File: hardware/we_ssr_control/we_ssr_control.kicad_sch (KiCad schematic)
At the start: 6 parts

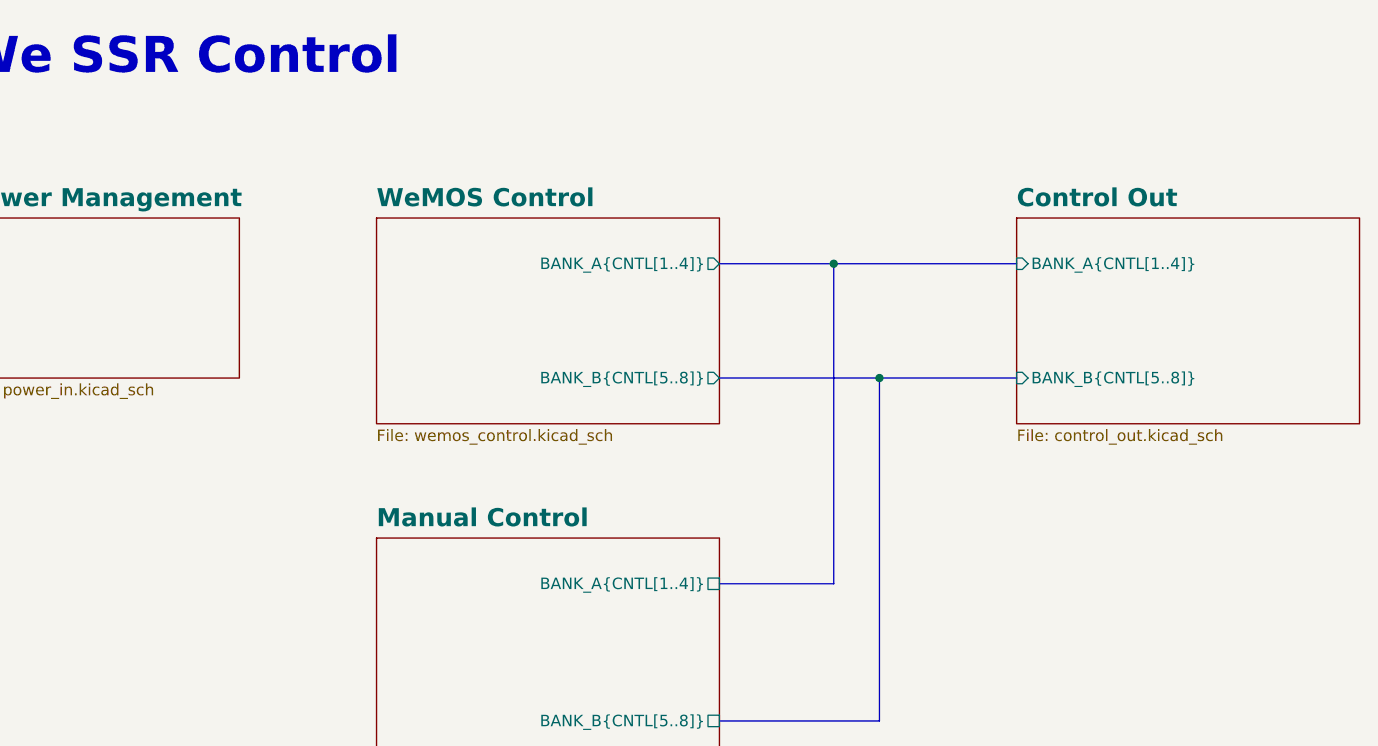
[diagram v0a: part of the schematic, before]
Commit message: Power supply changes plus misc.
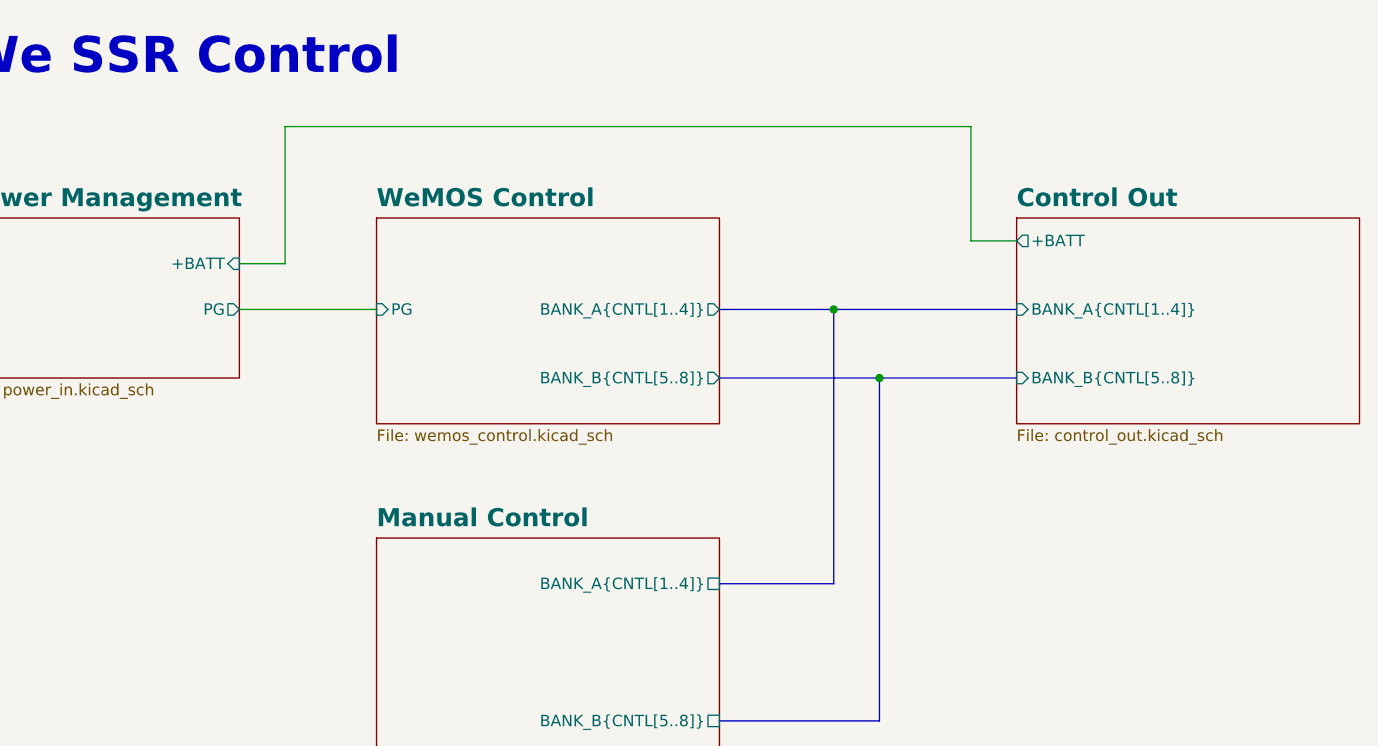
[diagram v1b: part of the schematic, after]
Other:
- sheet Control Out ports: added +BATT; removed none
- sheet Power Management ports: added +BATT, PG; removed none
- sheet WeMOS Control ports: added PG; removed none

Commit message: Pre KiCad 7.0.0 WIP
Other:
- sheet Control Out ports: added BANK_A{OUT[1..4]}, BANK_B{OUT[5..8]}; removed BANK_A{CNTL[1..4]}, BANK_B{CNTL[5..8]}
- sheet Manual Control ports: added BANK_A{OUT[1..4]}, BANK_B{OUT[5..8]}; removed BANK_A{CNTL[1..4]}, BANK_B{CNTL[5..8]}
- sheet WeMOS Control ports: added BANK_A{OUT[1..4]}, BANK_B{OUT[5..8]}; removed BANK_A{CNTL[1..4]}, BANK_B{CNTL[5..8]}
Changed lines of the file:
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@@
   (junction (at 27.94 152.4) (diameter 0) (color 0 0 0 0)
   )
-  (junction (at 111.76 45.72) (diameter 0) (color 0 0 0 0)
-  )
-  (junction (at 116.84 53.34) (diameter 0) (color 0 0 0 0)
+  (junction (at 111.76 45.72) (diameter 0) (color 255 255 0 1)
+  )
+  (junction (at 116.84 53.34) (diameter 0) (color 255 255 0 1)
   )
   (junction (at 27.94 157.48) (diameter 0) (color 0 0 0 0)
@@
   )
   (bus (pts (xy 99.06 45.72) (xy 111.76 45.72))
-    (stroke (width 0) (type default) (color 0 0 0 0))
+    (stroke (width 0) (type default) (color 255 255 0 1))
   )
   (wire (pts (xy 127 38.1) (xy 127 25.4))
@@
   )
   (bus (pts (xy 111.76 45.72) (xy 132.08 45.72))
-    (stroke (width 0) (type default) (color 0 0 0 0))
+    (stroke (width 0) (type default) (color 255 255 0 1))
   )
   (polyline (pts (xy 40.64 172.72) (xy 40.64 195.58))
@@
   )
   (bus (pts (xy 99.06 53.34) (xy 116.84 53.34))
-    (stroke (width 0) (type default) (color 0 0 0 0))
+    (stroke (width 0) (type default) (color 255 255 0 1))
   )
   (polyline (pts (xy 63.5 129.54) (xy 63.5 200.66))
@@
   )
   (bus (pts (xy 99.06 76.2) (xy 111.76 76.2))
-    (stroke (width 0) (type default) (color 0 0 0 0))
+    (stroke (width 0) (type default) (color 255 255 0 1))
   )
   (bus (pts (xy 116.84 91.44) (xy 116.84 53.34))
-    (stroke (width 0) (type default) (color 0 0 0 0))
+    (stroke (width 0) (type default) (color 255 255 0 1))
   )
   (polyline (pts (xy 63.5 200.66) (xy 15.24 200.66))
@@
   )
   (bus (pts (xy 116.84 53.34) (xy 132.08 53.34))
-    (stroke (width 0) (type default) (color 0 0 0 0))
+    (stroke (width 0) (type default) (color 255 255 0 1))
   )
   (polyline (pts (xy 45.72 137.16) (xy 45.72 167.64))
@@
   )
   (bus (pts (xy 99.06 91.44) (xy 116.84 91.44))
-    (stroke (width 0) (type default) (color 0 0 0 0))
+    (stroke (width 0) (type default) (color 255 255 0 1))
   )
   (bus (pts (xy 111.76 76.2) (xy 111.76 45.72))
-    (stroke (width 0) (type default) (color 0 0 0 0))
+    (stroke (width 0) (type default) (color 255 255 0 1))
   )
   (wire (pts (xy 27.94 147.32) (xy 27.94 152.4))
@@
       (effects (font (size 1.27 1.27)) (justify left top))
     )
-    (pin "BANK_B{CNTL[5..8]}" input (at 132.08 53.34 180)
-      (effects (font (size 1.27 1.27)) (justify left))
-    )
-    (pin "BANK_A{CNTL[1..4]}" input (at 132.08 45.72 180)
+    (pin "BANK_B{OUT[5..8]}" input (at 132.08 53.34 180)
+      (effects (font (size 1.27 1.27)) (justify left))
+    )
+    (pin "BANK_A{OUT[1..4]}" input (at 132.08 45.72 180)
       (effects (font (size 1.27 1.27)) (justify left))
     )
@@
       (effects (font (size 1.27 1.27)) (justify left top))
     )
-    (pin "BANK_A{CNTL[1..4]}" passive (at 99.06 76.2 0)
-      (effects (font (size 1.27 1.27)) (justify right))
-    )
-    (pin "BANK_B{CNTL[5..8]}" passive (at 99.06 91.44 0)
+    (pin "BANK_A{OUT[1..4]}" passive (at 99.06 76.2 0)
+      (effects (font (size 1.27 1.27)) (justify right))
+    )
+    (pin "BANK_B{OUT[5..8]}" passive (at 99.06 91.44 0)
       (effects (font (size 1.27 1.27)) (justify right))
     )
@@
       (effects (font (size 1.27 1.27)) (justify left top))
     )
-    (pin "BANK_A{CNTL[1..4]}" output (at 99.06 45.72 0)
-      (effects (font (size 1.27 1.27)) (justify right))
-    )
-    (pin "BANK_B{CNTL[5..8]}" output (at 99.06 53.34 0)
+    (pin "BANK_A{OUT[1..4]}" output (at 99.06 45.72 0)
+      (effects (font (size 1.27 1.27)) (justify right))
+    )
+    (pin "BANK_B{OUT[5..8]}" output (at 99.06 53.34 0)
       (effects (font (size 1.27 1.27)) (justify right))
     )
@@
     )
     (path "/a6fe8e39-c8fe-4793-ba2c-9e580a74c2e6/3fb71cbf-cff9-4475-be5c-cf772014cc05"
-      (reference "QD1") (unit 1) (value "2N7002K") (footprint "Package_TO_SOT_SMD:SOT-23-3")
+      (reference "QD1") (unit 1) (value "2N7002K") (footprint "dragon_mobile:2V7002KT1G")
     )
     (path "/a6fe8e39-c8fe-4793-ba2c-9e580a74c2e6/c9bf8404-861c-4866-b68d-e32ad5305808"
-      (reference "QD2") (unit 1) (value "2N7002K") (footprint "Package_TO_SOT_SMD:SOT-23-3")
+      (reference "QD2") (unit 1) (value "2N7002K") (footprint "dragon_mobile:2V7002KT1G")
     )
     (path "/a6fe8e39-c8fe-4793-ba2c-9e580a74c2e6/a5842628-7388-4ad5-b34a-936fbc4d3a6c"
-      (reference "QD3") (unit 1) (value "2N7002K") (footprint "Package_TO_SOT_SMD:SOT-23-3")
+      (reference "QD3") (unit 1) (value "2N7002K") (footprint "dragon_mobile:2V7002KT1G")
     )
     (path "/a6fe8e39-c8fe-4793-ba2c-9e580a74c2e6/7bdec03a-2a9c-450c-a12d-d9f73f34015c"
-      (reference "QD4") (unit 1) (value "2N7002K") (footprint "Package_TO_SOT_SMD:SOT-23-3")
+      (reference "QD4") (unit 1) (value "2N7002K") (footprint "dragon_mobile:2V7002KT1G")
     )
     (path "/a6fe8e39-c8fe-4793-ba2c-9e580a74c2e6/81e333b3-87dd-4483-aa95-abb876cf286a"
-      (reference "QD5") (unit 1) (value "2N7002K") (footprint "Package_TO_SOT_SMD:SOT-23-3")
+      (reference "QD5") (unit 1) (value "2N7002K") (footprint "dragon_mobile:2V7002KT1G")
     )
     (path "/a6fe8e39-c8fe-4793-ba2c-9e580a74c2e6/baa26d26-0263-475b-950b-61a0fd9bee77"
-      (reference "QD6") (unit 1) (value "2N7002K") (footprint "Package_TO_SOT_SMD:SOT-23-3")
+      (reference "QD6") (unit 1) (value "2N7002K") (footprint "dragon_mobile:2V7002KT1G")
     )
     (path "/a6fe8e39-c8fe-4793-ba2c-9e580a74c2e6/f7dd79dc-8801-4553-bcae-ecf432cbc728"
-      (reference "QD7") (unit 1) (value "2N7002K") (footprint "Package_TO_SOT_SMD:SOT-23-3")
+      (reference "QD7") (unit 1) (value "2N7002K") (footprint "dragon_mobile:2V7002KT1G")
     )
     (path "/a6fe8e39-c8fe-4793-ba2c-9e580a74c2e6/ba7065a3-89e0-4e78-85fc-07cce3926452"
-      (reference "QD8") (unit 1) (value "2N7002K") (footprint "Package_TO_SOT_SMD:SOT-23-3")
+      (reference "QD8") (unit 1) (value "2N7002K") (footprint "dragon_mobile:2V7002KT1G")
     )
     (path "/4ac8bdba-99f0-493b-92b7-7ade4e7be401/01be6298-46c7-4187-8bd6-d408dde519f7"
